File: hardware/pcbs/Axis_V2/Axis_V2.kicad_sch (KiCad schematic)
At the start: 51 parts, among them J1 EXT_SPI, J10 Conn_01x04, J2 EXT_I2C, J3 GPIO, J4 SWD, J5 UART, J6 HV_IDC, J7 Conn_01x02, J8 Conn_01x10, J9 Conn_01x02, SW1 RES, U1 FM24CL16B, U2 Pico, U3 MAX6107, U4 MAX31855EASA, U5 MAX31855EASA, U6 DS3231MZ, U7 TCA9534, U8 PCA9544AD, U9 ADS1119IPWR

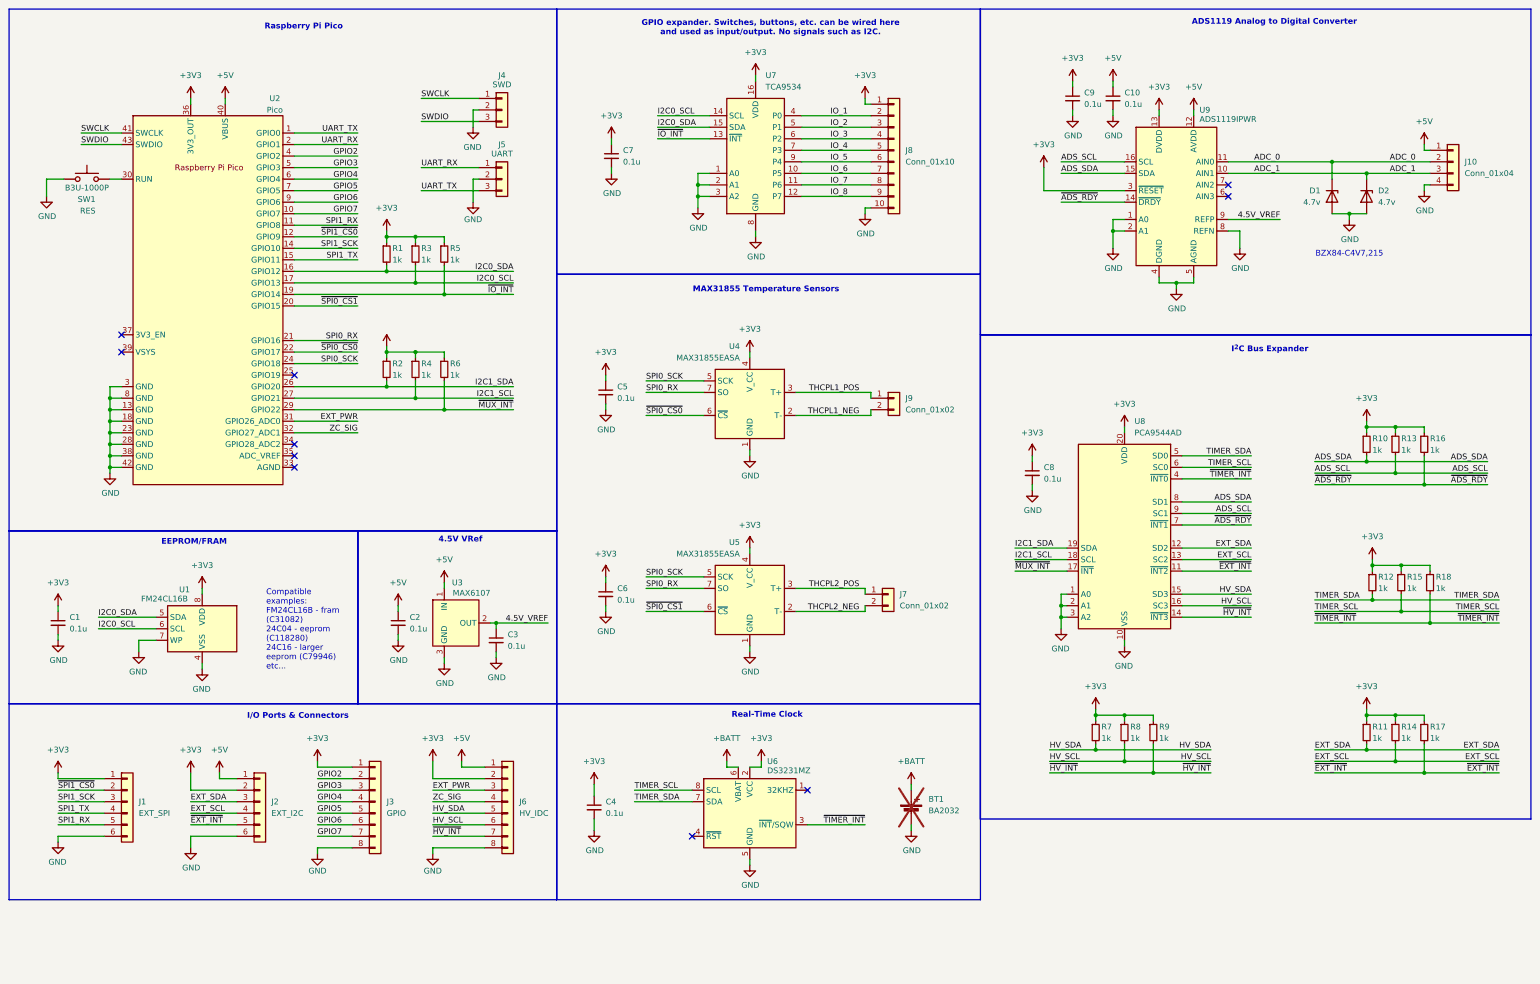
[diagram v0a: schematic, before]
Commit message: Almost done with v2, getting design review
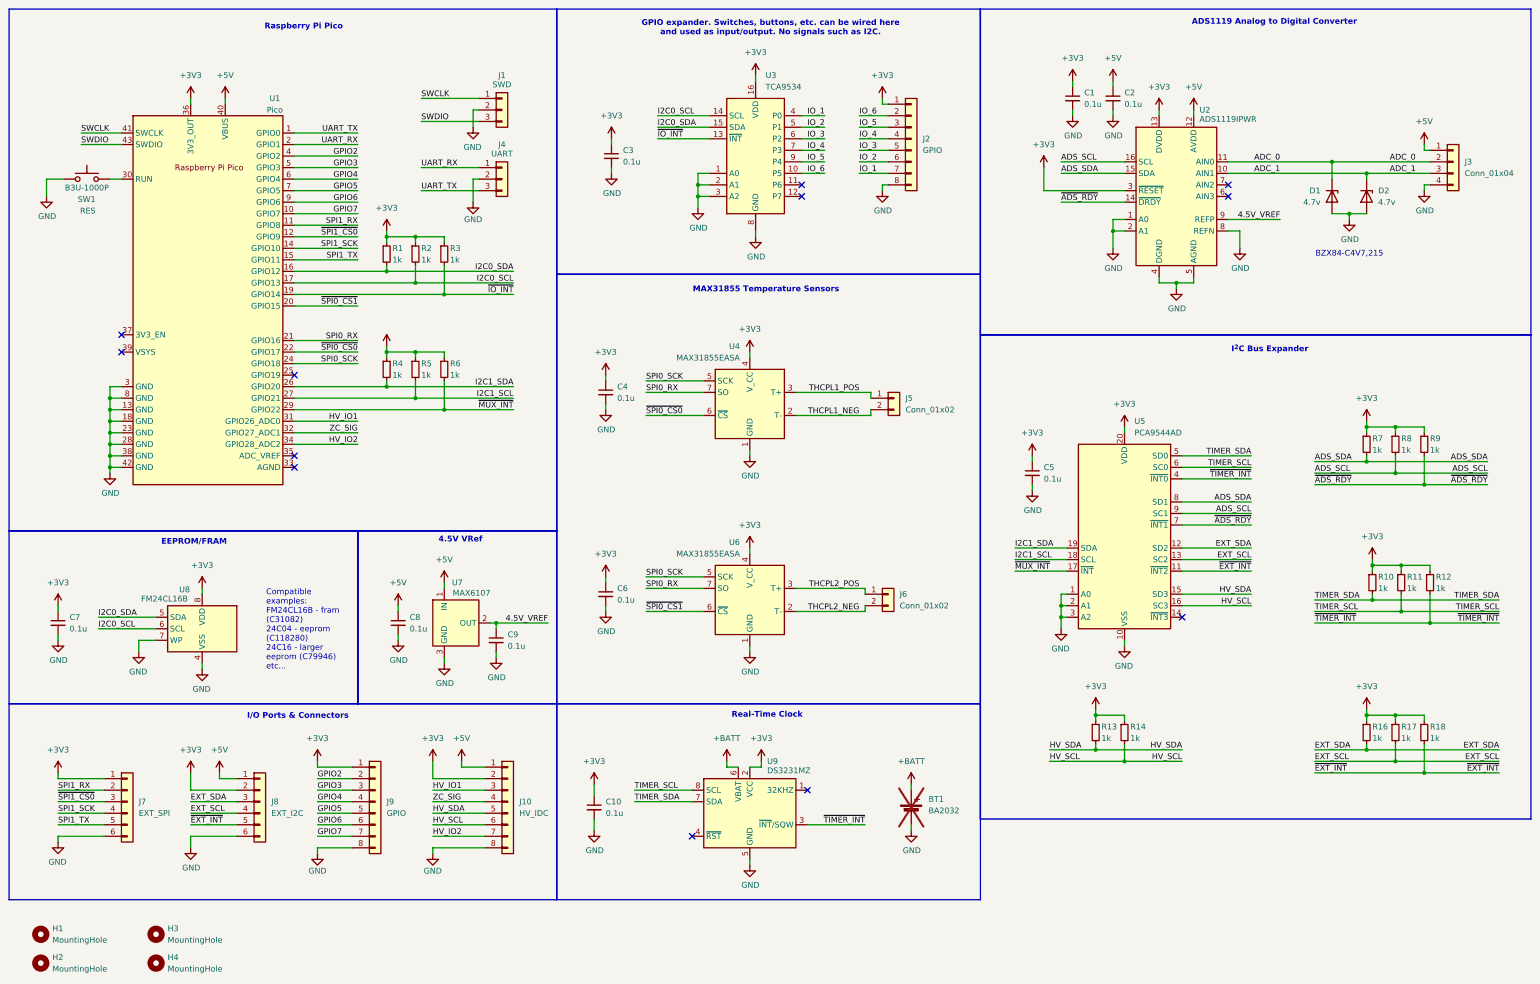
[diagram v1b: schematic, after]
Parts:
- removed J8: Conn_01x10, TerminalBlock_RND:TerminalBlock_RND_205-00240_1x10_P5.08mm_Horizontal, symbol Connector_Generic:Conn_01x10
- removed R9: 1k, Resistor_SMD:R_0603_1608Metric_Pad0.98x0.95mm_HandSolder, symbol Device:R_Small
- added H1, H2, H3, H4: MountingHole, MountingHole:MountingHole_2.7mm_M2.5, symbol Mechanical:MountingHole
- added J2: GPIO, TerminalBlock_Phoenix:TerminalBlock_Phoenix_MKDS-1,5-8-5.08_1x08_P5.08mm_Horizontal, symbol Connector_Generic:Conn_01x08
- J1: renamed from J4; footprint Connector_JST:JST_SH_BM03B-SRSS-TB_1x03-1MP_P1.00mm_Vertical -> Connector_JST:JST_SH_SM03B-SRSS-TB_1x03-1MP_P1.00mm_Horizontal
- J4: renamed from J5; footprint Connector_JST:JST_SH_BM03B-SRSS-TB_1x03-1MP_P1.00mm_Vertical -> Connector_JST:JST_SH_SM03B-SRSS-TB_1x03-1MP_P1.00mm_Horizontal
- J7: renamed from J1; footprint Connector_PinSocket_2.54mm:PinSocket_1x06_P2.54mm_Vertical -> Connector_PinHeader_2.54mm:PinHeader_1x06_P2.54mm_Vertical
- J8: renamed from J2; footprint Connector_PinSocket_2.54mm:PinSocket_1x06_P2.54mm_Vertical -> Connector_PinHeader_2.54mm:PinHeader_1x06_P2.54mm_Vertical
- J9: renamed from J3; footprint Connector_PinSocket_2.54mm:PinSocket_1x08_P2.54mm_Vertical -> Connector_PinHeader_2.54mm:PinHeader_1x08_P2.54mm_Vertical
- renumbered C9 to C1, C4 to C10, C10 to C2, C7 to C3, C5 to C4, C8 to C5, C1 to C7, C2 to C8, C3 to C9, J6 to J10, J10 to J3, J9 to J5, J7 to J6, R12 to R10, R15 to R11, R18 to R12, R7 to R13, R8 to R14, R11 to R16, R14 to R17, R17 to R18, R3 to R2, R5 to R3, R2 to R4, R4 to R5, R10 to R7, R13 to R8, R16 to R9, U2 to U1, U9 to U2, U7 to U3, U8 to U5, U5 to U6, U3 to U7, U1 to U8, U6 to U9
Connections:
- net +3V3: now also J2.1 (Pin_1)
- net GND: now also J2.8 (Pin_8)
- net IO_1: now also J2.7 (Pin_7)
- net IO_2: now also J2.6 (Pin_6)
- net IO_3: now also J2.5 (Pin_5)
- net IO_4: now also J2.4 (Pin_4)
- net IO_5: now also J2.3 (Pin_3)
- net IO_6: now also J2.2 (Pin_2)
- net SPI1_RX: now also J7.2 (Pin_2); no longer J7.5 (Pin_5)
- net SPI1_SCK: now also J7.4 (Pin_4); no longer J7.3 (Pin_3)
- net SPI1_TX: now also J7.5 (Pin_5); no longer J7.4 (Pin_4)
- net ~{SPI1_CS0}: now also J7.3 (Pin_3); no longer J7.2 (Pin_2)
- net HV_IO2: now reaches U1.34 (GPIO28_ADC2)
- net HV_IO2: now also J10.7 (Pin_7)
- net EXT_PWR renamed HV_IO1
- net IO_7: no longer names the net of U3.11 (P6)
- net IO_8: no longer names the net of U3.12 (P7)
- net ~{HV_INT}: no longer names the net of U5.14 (~{INT3})
- net ~{HV_INT}: no longer J10.7 (Pin_7)
- no-connect marks 10 -> 12
